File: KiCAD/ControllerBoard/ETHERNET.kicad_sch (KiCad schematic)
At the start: 38 parts, among them J2 RJ45-TRANSFO, U11 KSZ8081RNA, U15 SAME70_QFP144, Y2 25MHz

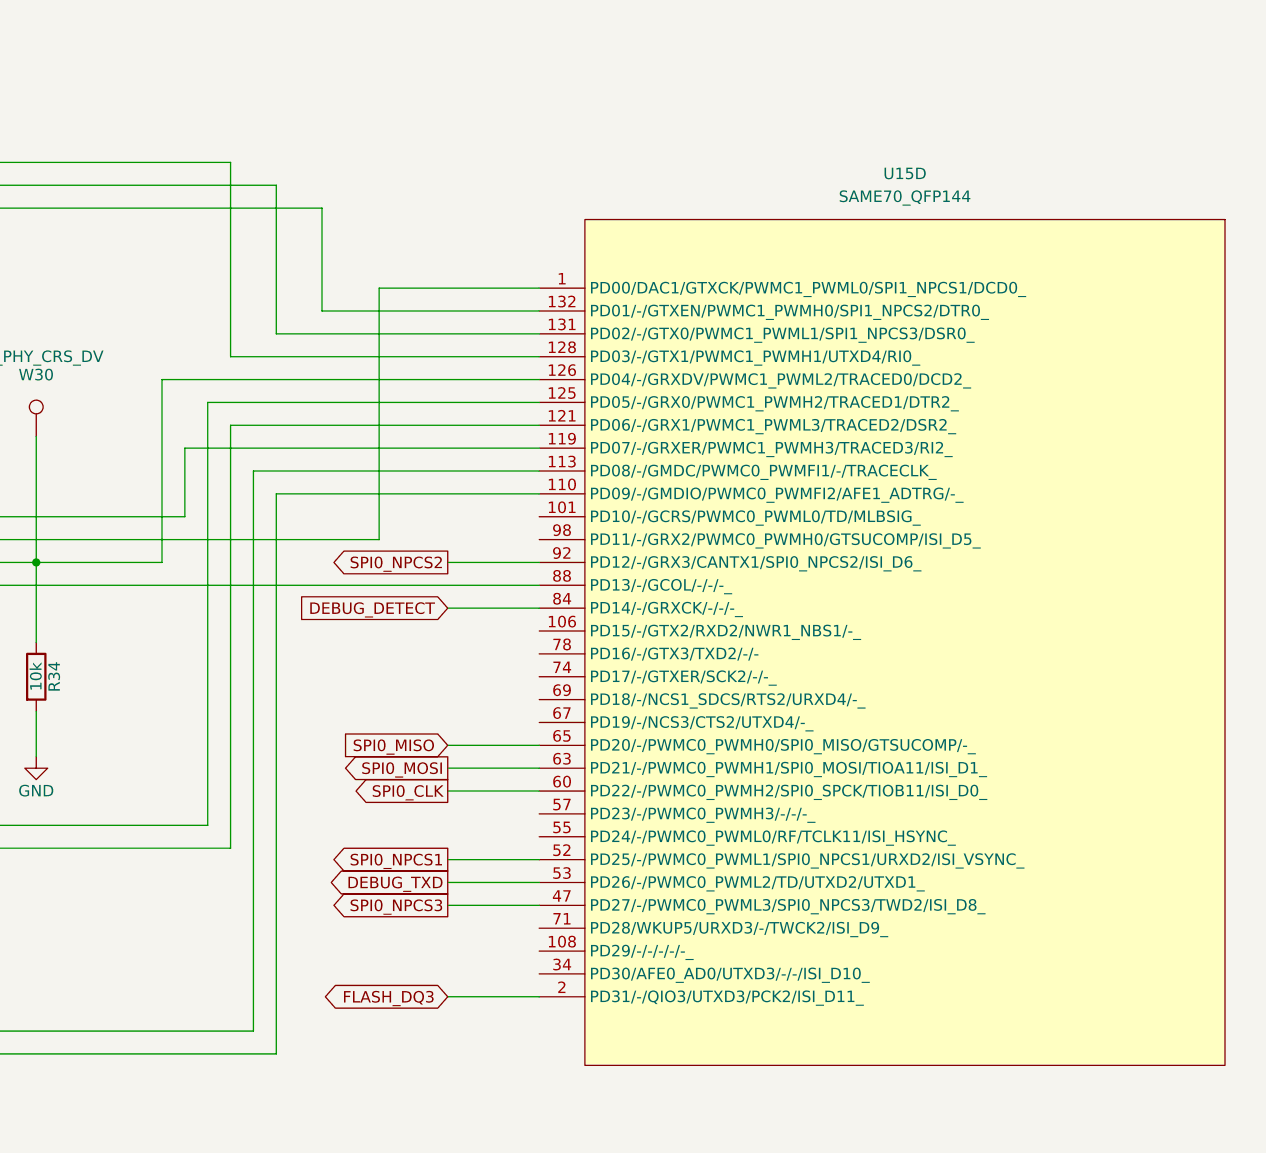
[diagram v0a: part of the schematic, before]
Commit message: CPU symbol changed, all pins on one page
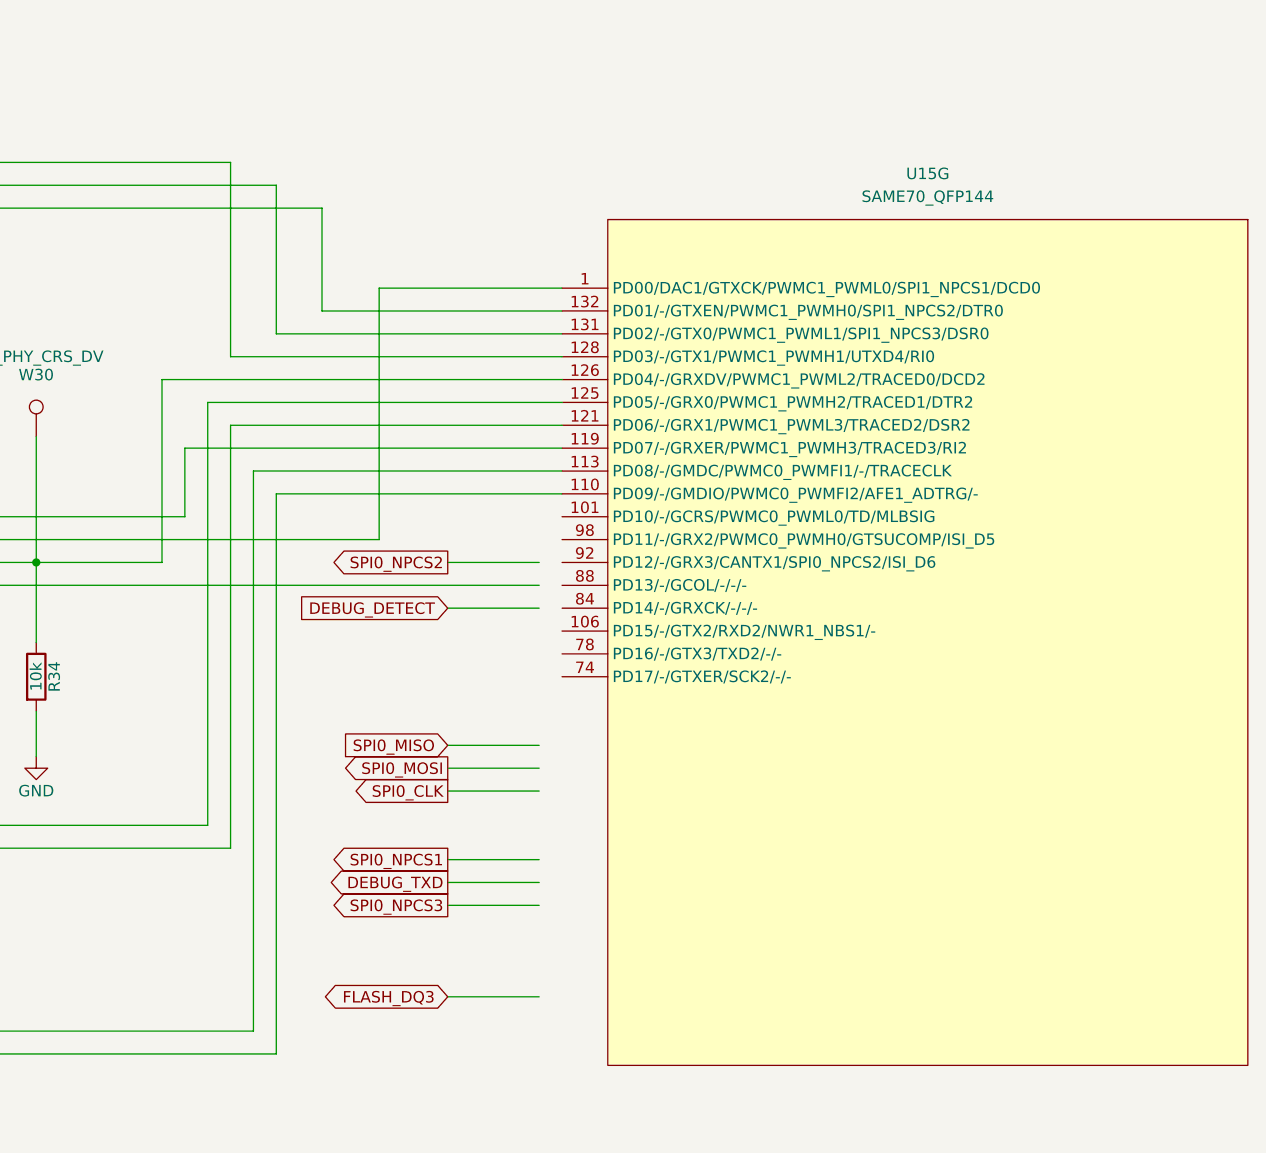
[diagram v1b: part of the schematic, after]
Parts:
- removed U15: SAME70_QFP144, Package_QFP:LQFP-144_20x20mm_P0.5mm, symbol ATSAME70:SAME70_QFP144
- added U15: SAME70_QFP144, Package_QFP:LQFP-144_20x20mm_P0.5mm, symbol ATSAME70:SAME70_QFP144
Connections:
- net at R33.2, U11.10 (MDIO), W22.1: now also U15.110 (PD09/-/GMDIO/PWMC0_PWMFI2/AFE1_ADTRG/-)
- net at U11.11 (MDC), W23.1: now also U15.113 (PD08/-/GMDC/PWMC0_PWMFI1/-/TRACECLK)
- net at U11.12 (RXD1), W33.1: now also U15.121 (PD06/-/GRX1/PWMC1_PWML3/TRACED2/DSR2)
- net at U11.13 (RXD0), W29.1: now also U15.125 (PD05/-/GRX0/PWMC1_PWMH2/TRACED1/DTR2)
- net at R34.1, U11.15 (CRS_DV/PHYAD[1,0]), W30.1: now also U15.126 (PD04/-/GRXDV/PWMC1_PWML2/TRACED0/DCD2)
- net at U11.17 (RXER), W27.1: now also U15.119 (PD07/-/GRXER/PWMC1_PWMH3/TRACED3/RI2)
- net at U11.19 (TXEN), W31.1: now also U15.132 (PD01/-/GTXEN/PWMC1_PWMH0/SPI1_NPCS2/DTR0)
- net at U11.20 (TXD0), W28.1: now also U15.131 (PD02/-/GTX0/PWMC1_PWML1/SPI1_NPCS3/DSR0)
- net at U11.21 (TXD1), W25.1: now also U15.128 (PD03/-/GTX1/PWMC1_PWMH1/UTXD4/RI0)
- net at R35.1, W24.1: now also U15.1 (PD00/DAC1/GTXCK/PWMC1_PWML0/SPI1_NPCS1/DCD0)
